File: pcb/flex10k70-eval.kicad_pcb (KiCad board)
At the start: 2 copper layers, 80 x 145 mm, 68 parts, among them CN1 IO_1, CN2 IO_2, CN3 IO_3, CN4 IO_4, CN5 FLASH, CN6 JTAG, SW1 SW_DIP_x04, SW2 SW_DIP_x04, U1 25LC1024-I/SM, U2 EPF10K70RC240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

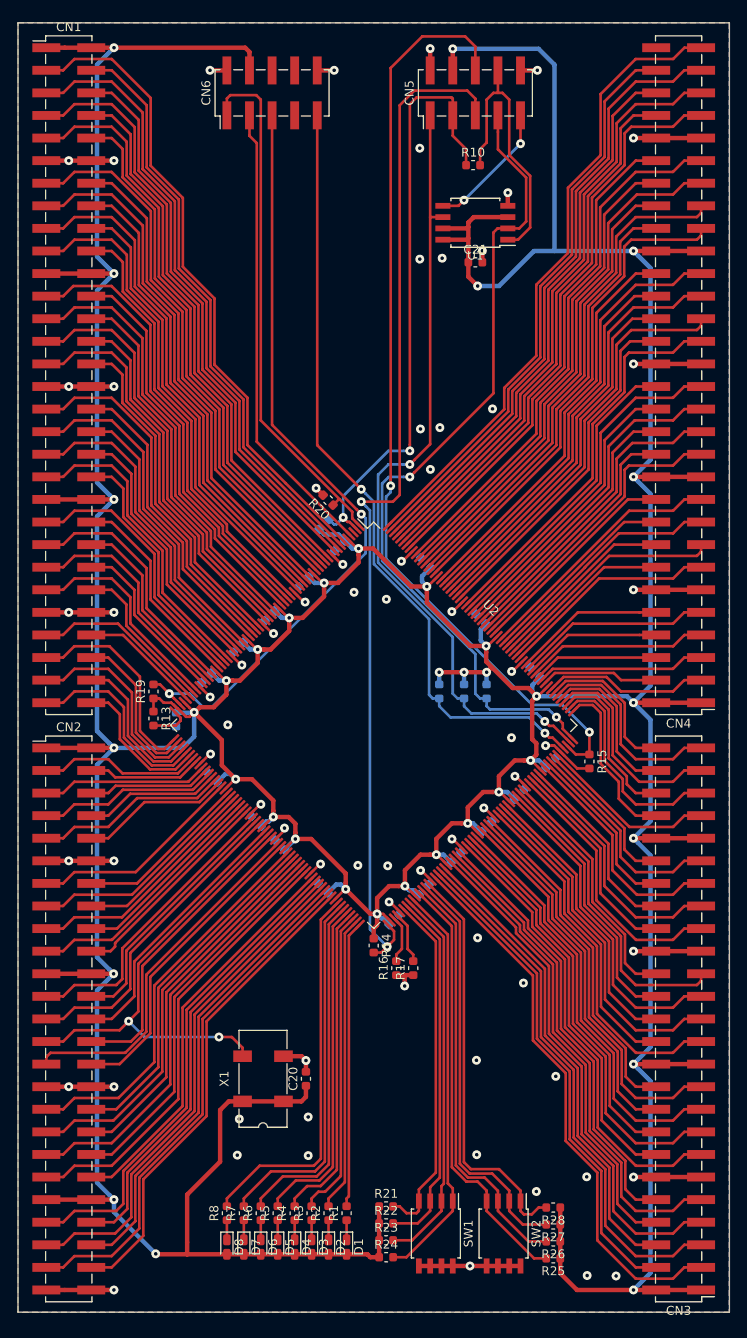
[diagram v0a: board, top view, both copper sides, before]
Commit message: modify CN3 CN4 pin orientation
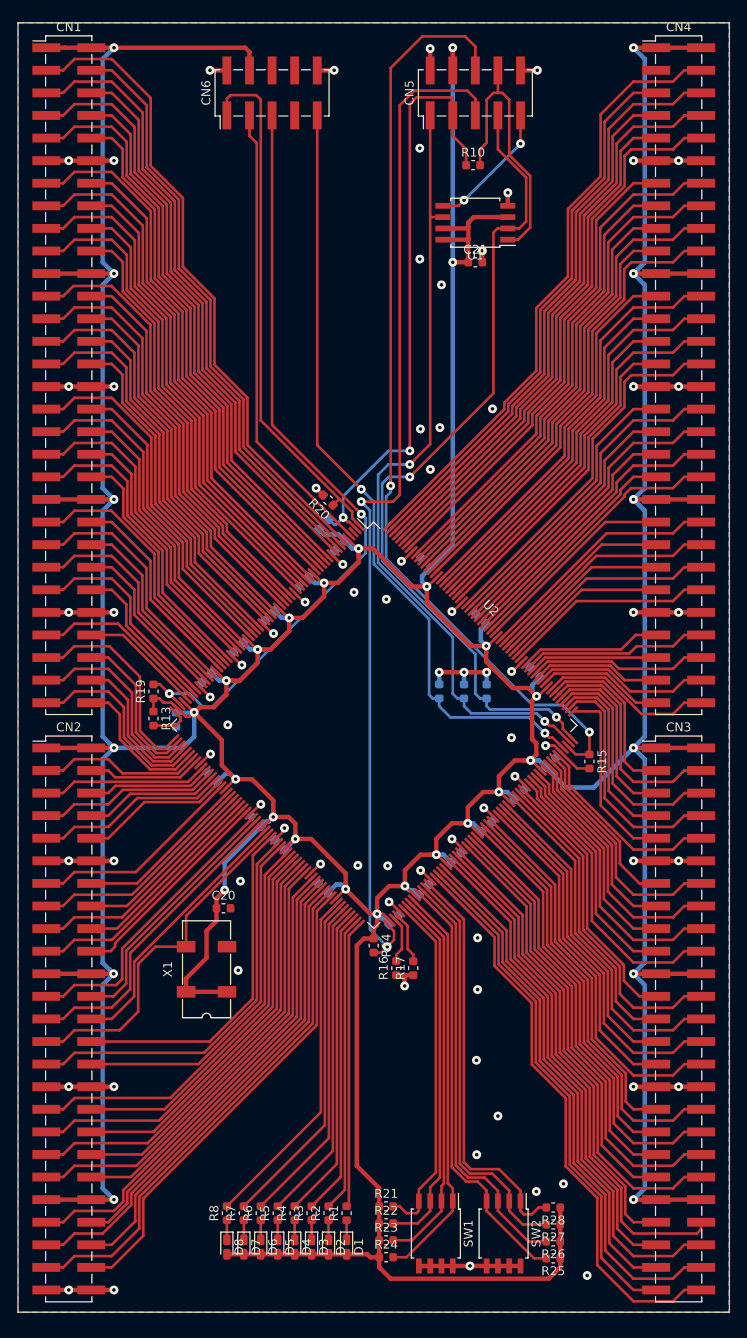
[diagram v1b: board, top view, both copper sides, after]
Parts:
- moved C20 21.3 mm to (85.5, 122.2), turned to 0 degrees
- moved X1 13.9 mm to (83.6, 129.0)
- turned CN3 to 0 degrees
- turned CN4 to 0 degrees
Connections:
- CN3 pad 10: /PIN_144 -> /PIN_175
- CN3 pad 13: /PIN_146 -> /PIN_174
- CN3 pad 14: /PIN_147 -> /PIN_173
- CN3 pad 15: /PIN_148 -> /PIN_172
- CN3 pad 16: /PIN_149 -> /PIN_171
- CN3 pad 17: /PIN_151 -> /PIN_169
- CN3 pad 18: /PIN_152 -> /PIN_168
- CN3 pad 19: /PIN_153 -> /PIN_167
- CN3 pad 20: /PIN_154 -> /PIN_166
- CN3 pad 23: /PIN_156 -> /PIN_164
- CN3 pad 24: /PIN_157 -> /PIN_163
- CN3 pad 25: /PIN_158 -> /PIN_162
- CN3 pad 26: /PIN_159 -> /PIN_161
- CN3 pad 27: /PIN_161 -> /PIN_159
- CN3 pad 28: /PIN_162 -> /PIN_158
- CN3 pad 29: /PIN_163 -> /PIN_157
- CN3 pad 3: /PIN_136 -> /PIN_187
- CN3 pad 30: /PIN_164 -> /PIN_156
- CN3 pad 33: /PIN_166 -> /PIN_154
- CN3 pad 34: /PIN_167 -> /PIN_153
- CN3 pad 35: /PIN_168 -> /PIN_152
- CN3 pad 36: /PIN_169 -> /PIN_151
- CN3 pad 37: /PIN_171 -> /PIN_149
- CN3 pad 38: /PIN_172 -> /PIN_148
- CN3 pad 39: /PIN_173 -> /PIN_147
- CN3 pad 4: /PIN_137 -> /PIN_186
- CN3 pad 40: /PIN_174 -> /PIN_146
- CN3 pad 43: /PIN_175 -> /PIN_144
- CN3 pad 44: /PIN_181 -> /PIN_143
- CN3 pad 45: /PIN_182 -> /PIN_142
- CN3 pad 46: /PIN_183 -> /PIN_141
- CN3 pad 47: /PIN_184 -> /PIN_139
- CN3 pad 48: /PIN_185 -> /PIN_138
- CN3 pad 49: /PIN_186 -> /PIN_137
- CN3 pad 5: /PIN_138 -> /PIN_185
- CN3 pad 50: /PIN_187 -> /PIN_136
- CN3 pad 6: /PIN_139 -> /PIN_184
- CN3 pad 7: /PIN_141 -> /PIN_183
- CN3 pad 8: /PIN_142 -> /PIN_182
- CN3 pad 9: /PIN_143 -> /PIN_181
- CN4 pad 10: /PIN_196 -> /PIN_234
- CN4 pad 13: /PIN_198 -> /PIN_233
- CN4 pad 14: /PIN_199 -> /PIN_231
- CN4 pad 15: /PIN_200 -> /PIN_230
- CN4 pad 16: /PIN_201 -> /PIN_229
- CN4 pad 17: /PIN_202 -> /PIN_228
- CN4 pad 18: /PIN_203 -> /PIN_227
- CN4 pad 19: /PIN_204 -> /PIN_226
- CN4 pad 20: /PIN_206 -> /PIN_225
- CN4 pad 23: /PIN_207 -> /PIN_223
- CN4 pad 24: /PIN_208 -> /PIN_222
- CN4 pad 25: /PIN_209 -> /PIN_221
- CN4 pad 26: /PIN_210 -> /PIN_220
- CN4 pad 27: /PIN_211 -> /PIN_219
- CN4 pad 28: /PIN_212 -> /PIN_218
- CN4 pad 29: /PIN_213 -> /PIN_217
- CN4 pad 3: /PIN_188 -> (no net)
- CN4 pad 30: /PIN_214 -> /PIN_215
- CN4 pad 33: /PIN_215 -> /PIN_214
- CN4 pad 34: /PIN_217 -> /PIN_213
- CN4 pad 35: /PIN_218 -> /PIN_212
- CN4 pad 36: /PIN_219 -> /PIN_211
- CN4 pad 37: /PIN_220 -> /PIN_210
- CN4 pad 38: /PIN_221 -> /PIN_209
- CN4 pad 39: /PIN_222 -> /PIN_208
- CN4 pad 4: /PIN_190 -> /PIN_240
- CN4 pad 40: /PIN_223 -> /PIN_207
- CN4 pad 43: /PIN_225 -> /PIN_206
- CN4 pad 44: /PIN_226 -> /PIN_204
- CN4 pad 45: /PIN_227 -> /PIN_203
- CN4 pad 46: /PIN_228 -> /PIN_202
- CN4 pad 47: /PIN_229 -> /PIN_201
- CN4 pad 48: /PIN_230 -> /PIN_200
- CN4 pad 49: /PIN_231 -> /PIN_199
- CN4 pad 5: /PIN_191 -> /PIN_239
- CN4 pad 50: /PIN_233 -> /PIN_198
- CN4 pad 53: /PIN_234 -> /PIN_196
- CN4 pad 54: /PIN_235 -> /PIN_195
- CN4 pad 55: /PIN_236 -> /PIN_194
- CN4 pad 56: /PIN_237 -> /PIN_193
- CN4 pad 57: /PIN_238 -> /PIN_192
- CN4 pad 58: /PIN_239 -> /PIN_191
- CN4 pad 59: /PIN_240 -> /PIN_190
- CN4 pad 6: /PIN_192 -> /PIN_238
- CN4 pad 60: (no net) -> /PIN_188
- CN4 pad 7: /PIN_193 -> /PIN_237
- CN4 pad 8: /PIN_194 -> /PIN_236
- CN4 pad 9: /PIN_195 -> /PIN_235
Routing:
- net +5V: track 781.6 -> 823.3 mm
- net /PIN_91: track 52.8 -> 39.8 mm, vias 2 -> 0
- net /PIN_92: track 34.1 -> 39.3 mm
- net /PIN_95: track 35.2 -> 40.4 mm
- net /PIN_94: track 40.6 -> 45.3 mm
- net GND: track 149.6 -> 145.6 mm, vias 70 -> 72
- net /PIN_113: track 42.9 -> 39.3 mm
- net /PIN_97: track 44.1 -> 47.5 mm
- net /PIN_98: track 39.5 -> 42.7 mm
- net /PIN_143: track 56.2 -> 59.3 mm
- net /PIN_218: track 46.8 -> 43.6 mm
- net /PIN_225: track 55.5 -> 52.5 mm
- net /PIN_99: track 45.9 -> 48.9 mm
- net /PIN_114: track 41.2 -> 38.3 mm
- net /PIN_227: track 57.3 -> 54.5 mm
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
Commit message: modify GND via
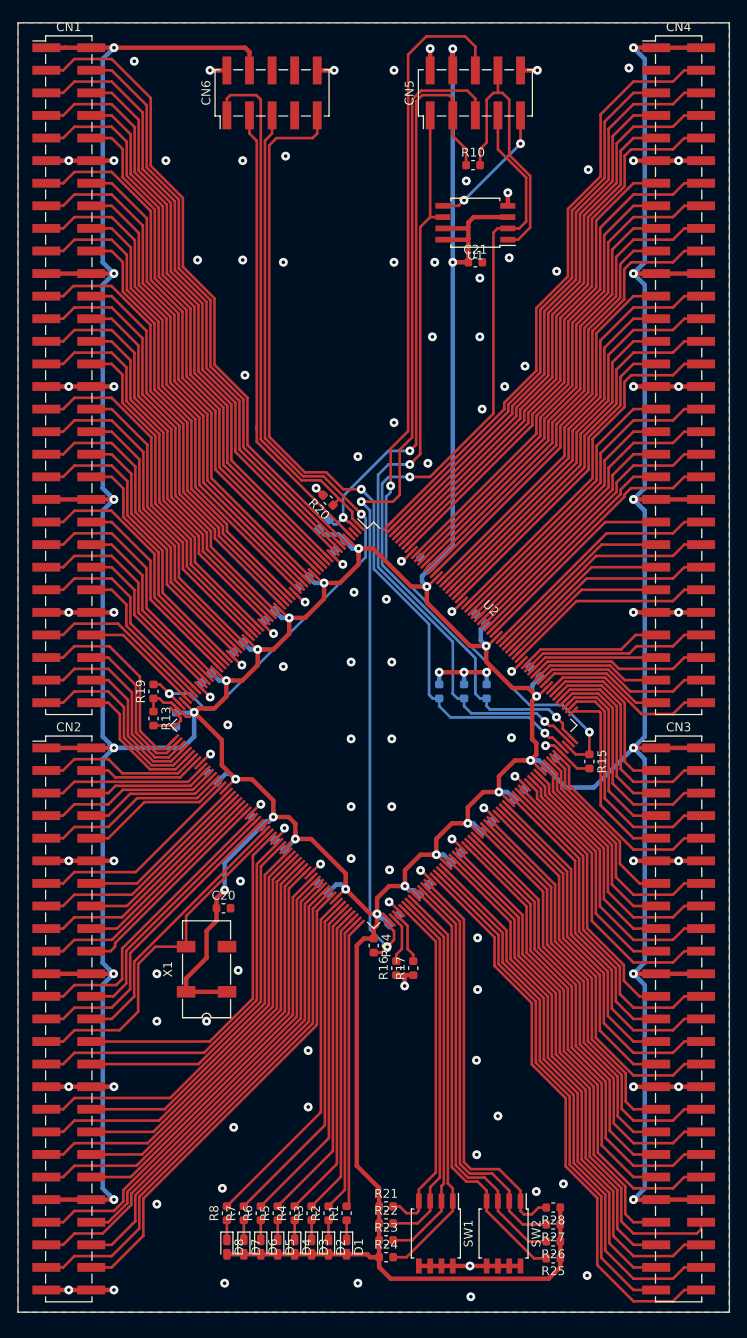
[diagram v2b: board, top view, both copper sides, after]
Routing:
- net /TDI: track 88.5 -> 98.0 mm
- net /TMS: track 87.5 -> 90.0 mm
- net /DATA0: track 94.2 -> 95.5 mm
- net GND: track 145.6 -> 144.3 mm, vias 72 -> 107
- net /TCK: track 59.6 -> 60.9 mm

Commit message: modify gnd via, silk, plot gerber, drill
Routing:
- net GND: vias 107 -> 121
